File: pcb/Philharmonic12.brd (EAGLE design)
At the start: 97.8 x 95.2 mm, 45 parts, among them IC1 MC6821, IC2 AY-3-8910-RP, IC3 AY-3-8910-RP, IC4 AY-3-8910-RP, IC5 AY-3-8910-RP, IC6 74LS138N, IC7 74ALS30N, IC8 LM386N-1, IC9 LM386N-1, X1 EXPANSION_PORT_COCO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

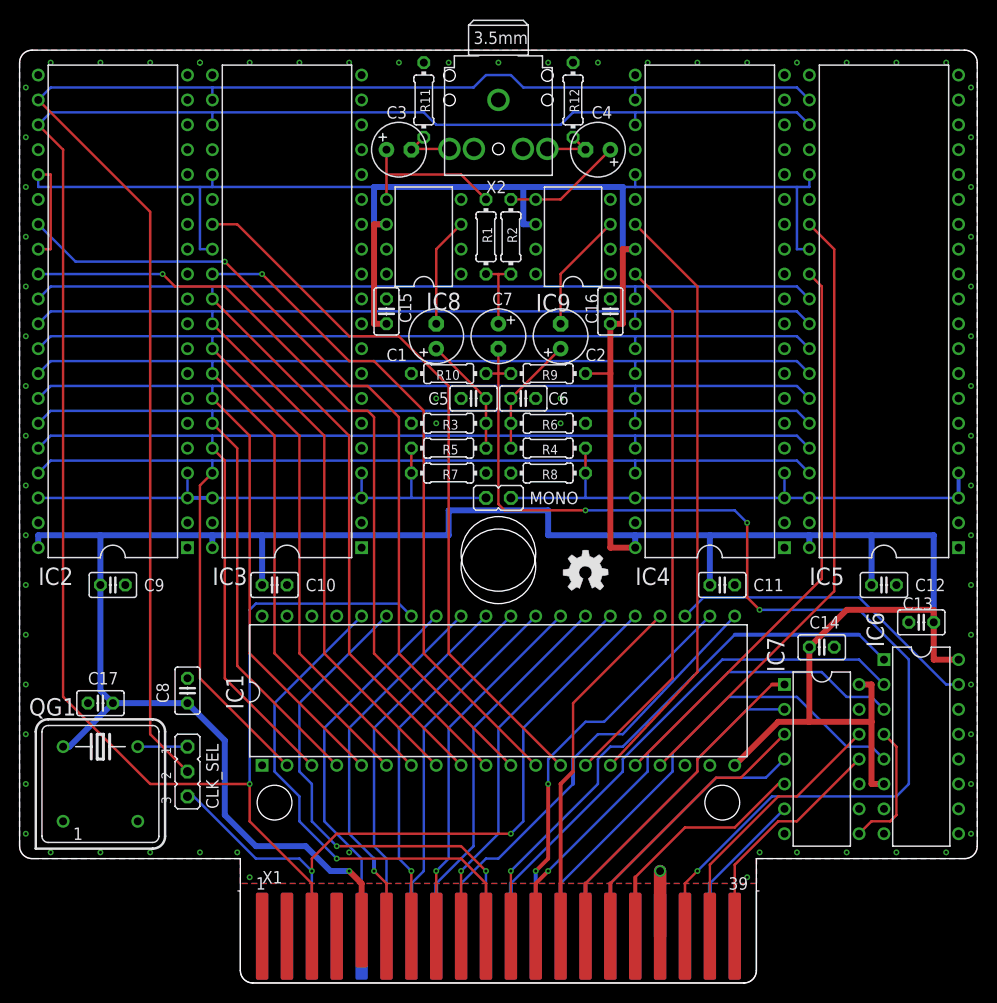
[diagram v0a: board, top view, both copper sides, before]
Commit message: Can't get .895MHz oscillators, so modified to use 3.59MHz and /4 divider.
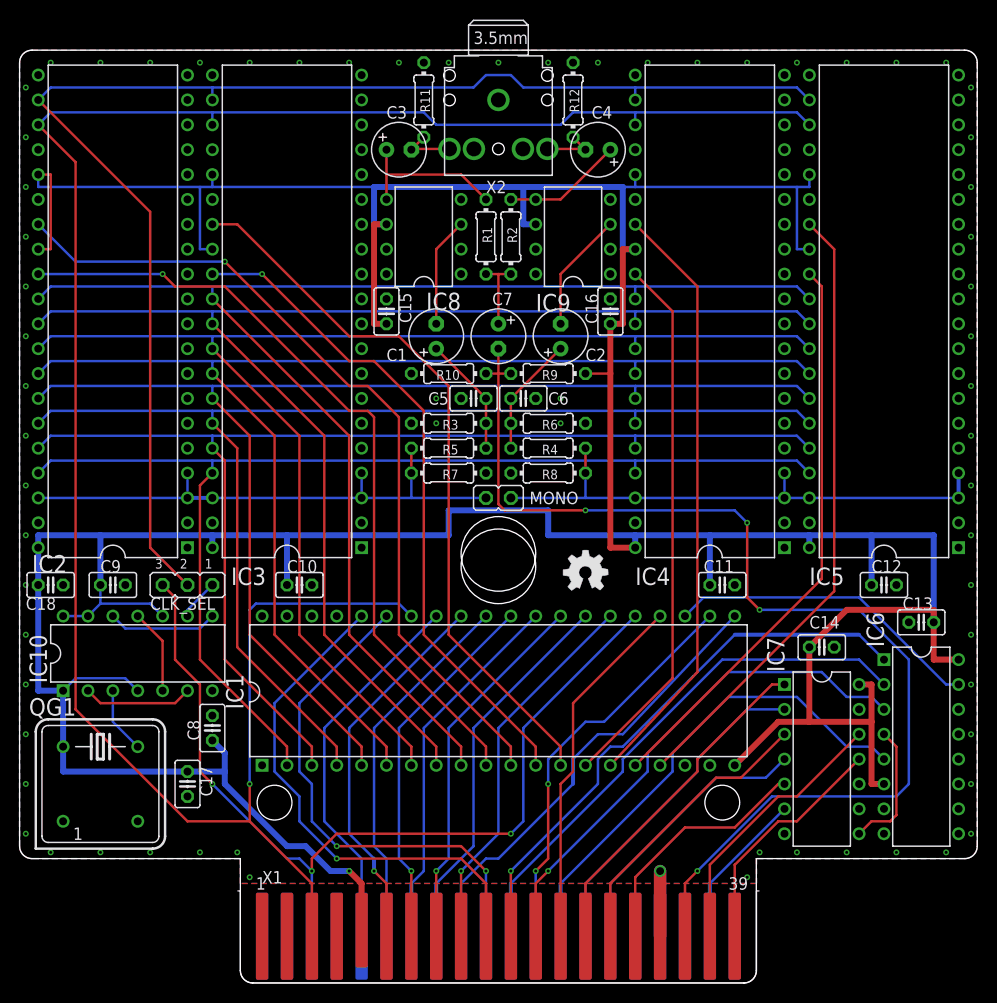
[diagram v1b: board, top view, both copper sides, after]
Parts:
- added C18: (no value), rcl:C025-025X050
- added IC10: 74LS74N, 74xx-us-jlb:DIL14-RP
- QG1: value .895MHz -> 3.579545MHz
- moved CLK_SEL 19.1 mm to (-31.8, 40.6), turned to 180 degrees
- moved C17 12.1 mm to (-31.8, 20.3), turned to 270 degrees
- moved C8 4.58 mm to (-29.2, 26.0)
- moved C10 2.54 mm to (-20.3, 40.6)
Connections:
- new net N$1: IC10.2, IC10.6
- new net N$10: IC10.11, IC10.5
- new net N$15: IC10.12, IC10.8
- new net N$17: CLK_SEL.1, IC10.9
- net GND: now also C18.2, IC10.7
- net N$4: now also IC10.3; no longer CLK_SEL.1
- net VCC: now also C18.1, IC10.1, IC10.10, IC10.13, IC10.14, IC10.4
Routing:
- net VCC: track 428.4 -> 458.3 mm
- net E: track 72.6 -> 93.0 mm, vias 2 -> 3
- net CLK_AUDIO: track 158.3 -> 139.2 mm
- net N$15: track 0.00 -> 11.2 mm
- net N$1: track 0.00 -> 11.2 mm
- net N$10: track 0.00 -> 8.67 mm
- net N$17: track 0.00 -> 4.23 mm
- net N$4: track 5.08 -> 6.77 mm
- net !RESET: track 218.8 -> 220.4 mm
- net GND: vias 70 -> 68

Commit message: Added parts values
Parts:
- C1, C2, C3, C4, C7: value (none) -> 4m7
- C10, C11, C12, C13, C14, C15, C16, C17, C18, C8, C9: value (none) -> .1u
- C5, C6: value (none) -> 220p
- R1, R2, R3, R4: value (none) -> 470
- R10, R11, R12, R9: value (none) -> 10K
- R5, R6: value (none) -> 4K7
- R7, R8: value (none) -> 1K

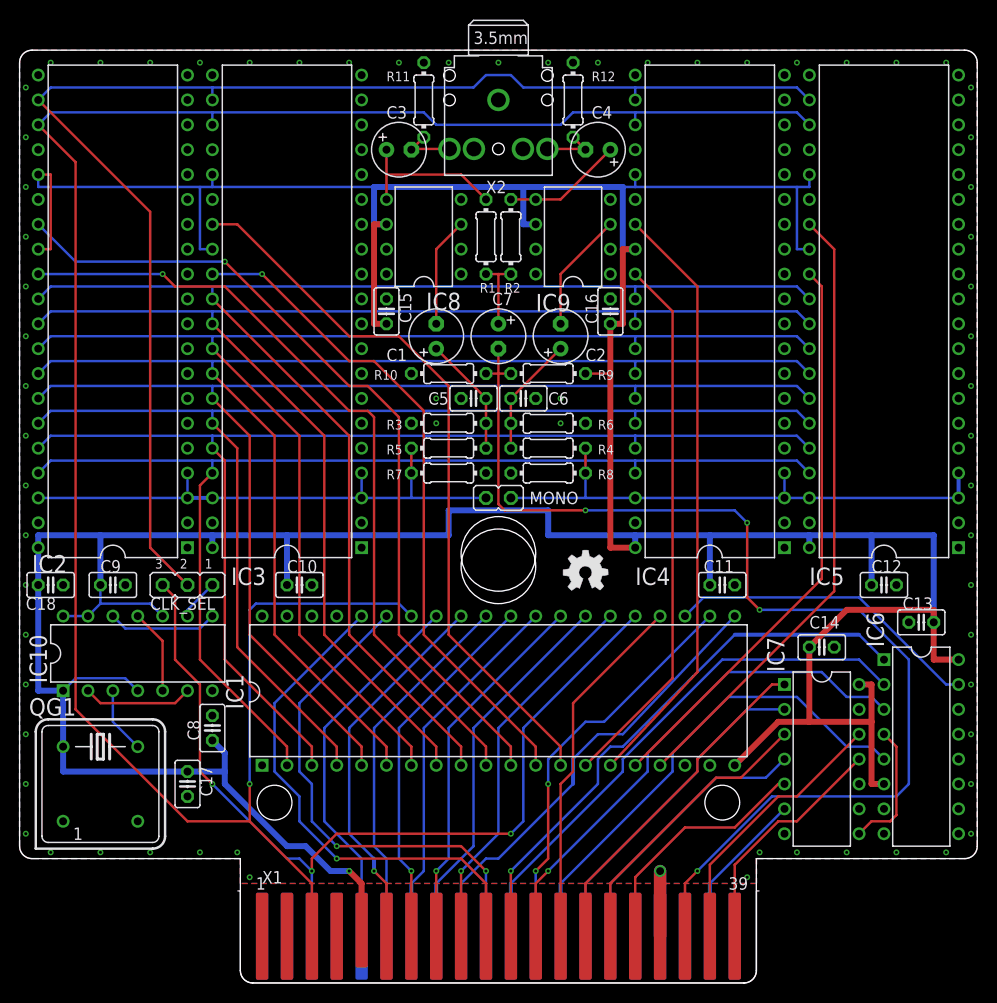
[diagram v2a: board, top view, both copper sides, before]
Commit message: Minor silkscreen updates
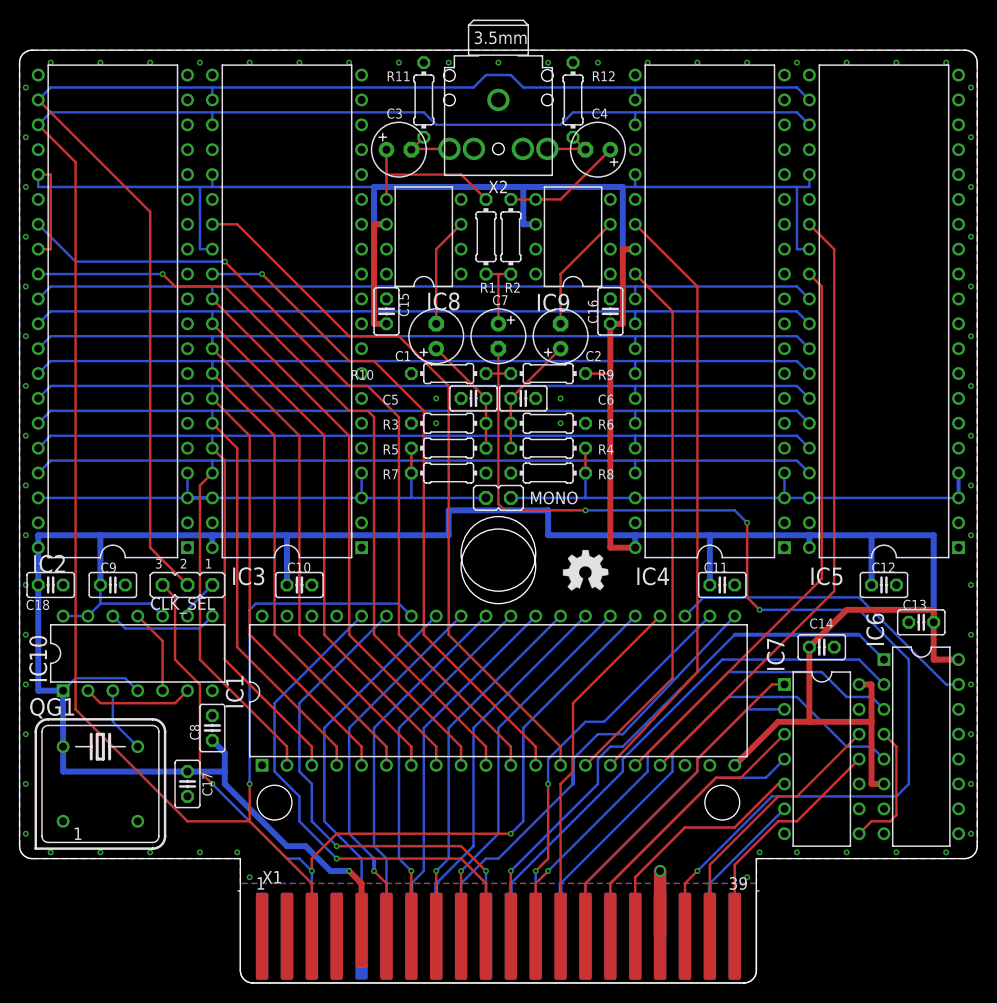
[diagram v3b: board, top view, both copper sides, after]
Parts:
- IC1: value MC6821 -> MC68B21
- IC7: value 74ALS30N -> 74LS30N
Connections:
- net N$10 renamed CLK/2
- net N$17 renamed CLK/4
- net N$4 renamed CLK
